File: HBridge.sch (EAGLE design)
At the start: 42 parts, among them IC1 74HC08D, IC2 A4954, J1 In 3/4, J2 Power, J3 In 1/2, J4 Output A, J5 Output B, J6 Digital_8_13, J7 Analog, J8 Digital_0_7

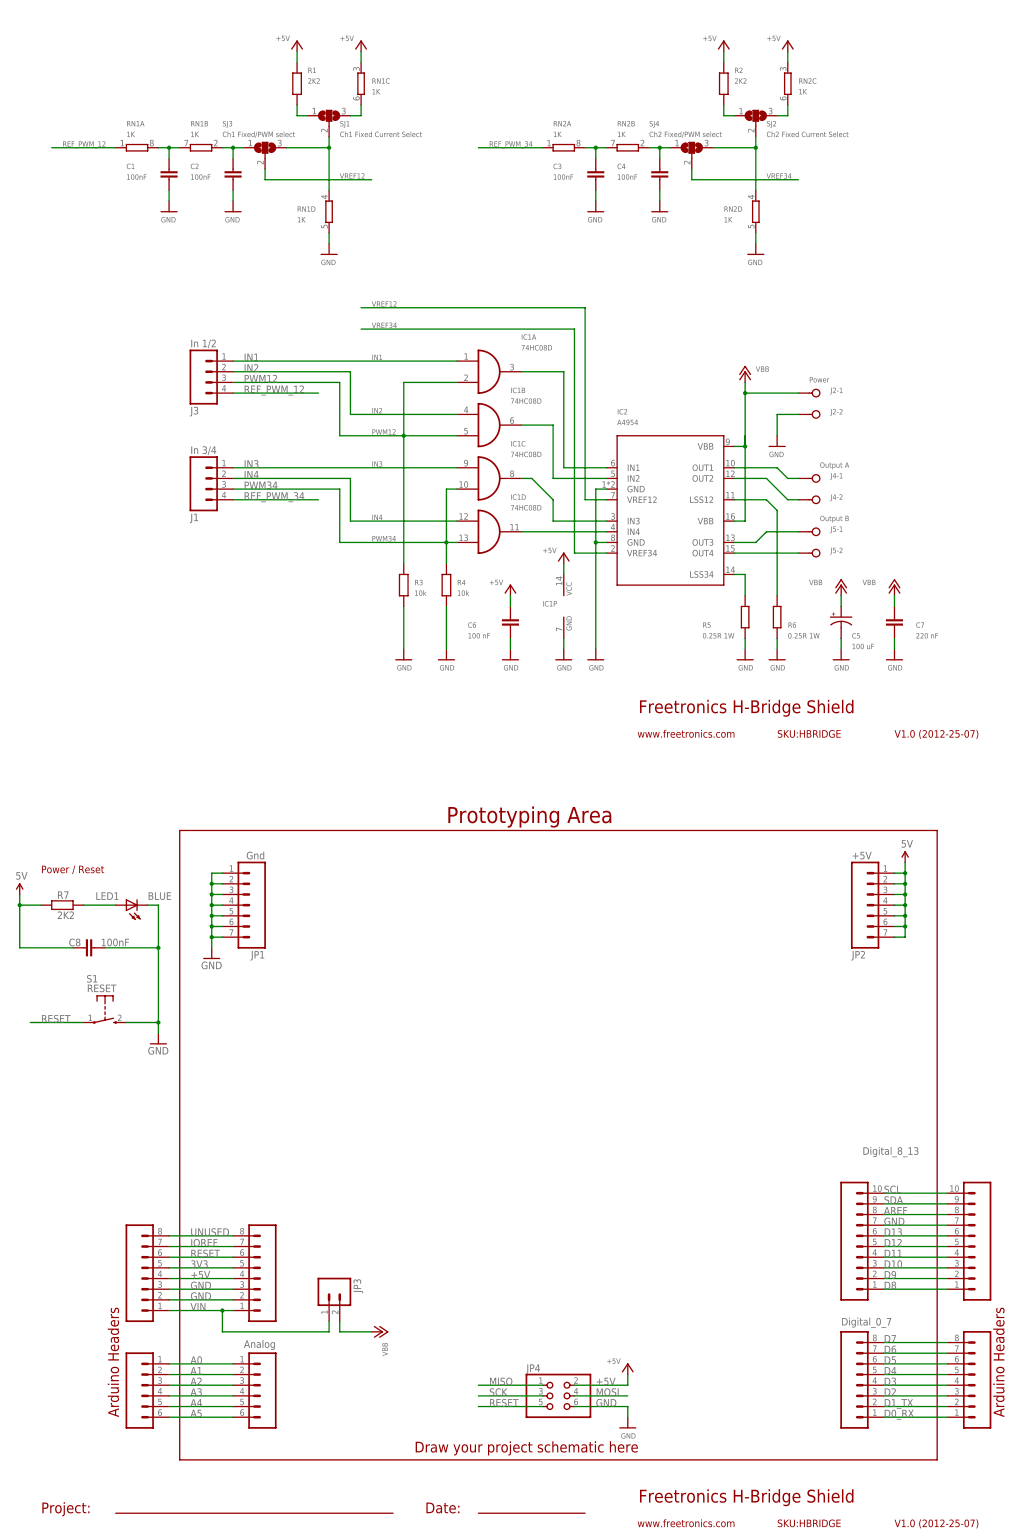
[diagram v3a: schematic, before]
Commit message: Made track widths consistent; renamed parts; relocated designators, improved silkscreen
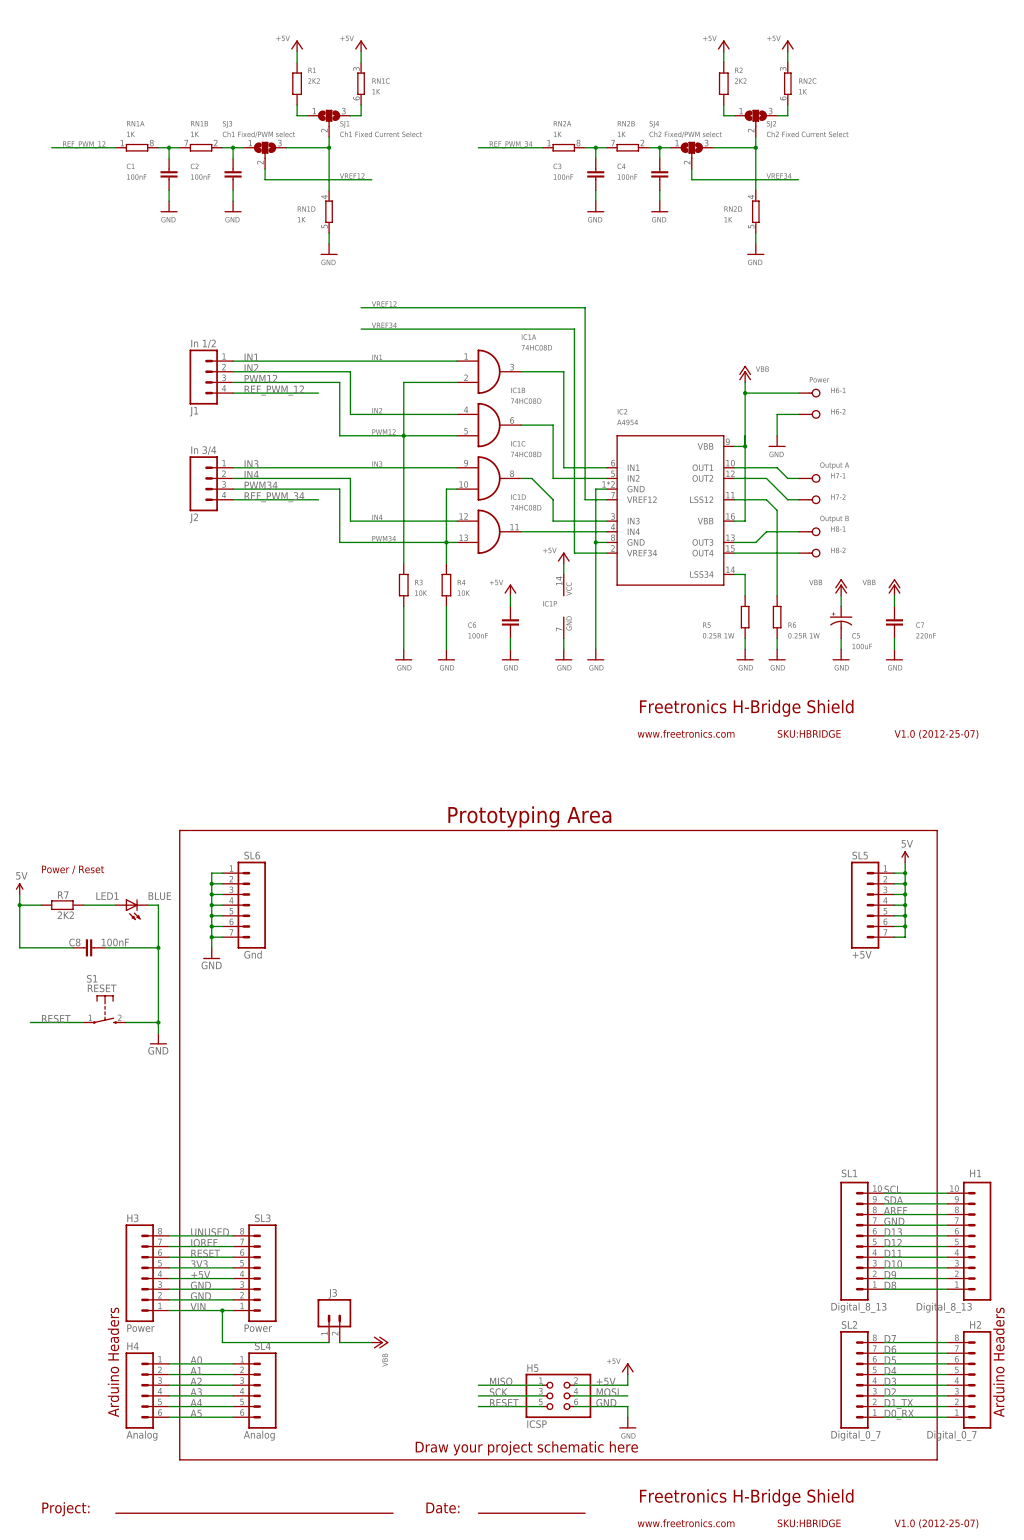
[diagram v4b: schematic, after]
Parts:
- removed JP2: +5V, SparkFun:M07
- removed JP3: (no value), freetronics-master-v1:M02PTH
- added H3: Power, freetronics:M08
- added H6: Power, con-wago-508:W237-02P
- C5: value 100 uF -> 100uF
- C6: value 100 nF -> 100nF
- C7: value 220 nF -> 220nF
- H5: value (none) -> ICSP
- J1: value In 3/4 -> In 1/2
- J2: value Power -> In 3/4; device con-wago-508:W237-02P -> freetronics-master-v1:M04PTH
- J3: value In 1/2 -> (none); device freetronics-master-v1:M04PTH -> freetronics-master-v1:M02PTH
- R3, R4: value 10k -> 10K
- SL2: value Analog -> Digital_0_7; device freetronics:M06SIP -> freetronics:M08
- SL3: value Digital_0_7 -> Power
- SL4: value Digital_0_7 -> Analog; device freetronics:M08 -> freetronics:M06SIP
- SL5: value Digital_0_7 -> +5V; device freetronics:M08 -> SparkFun:M07
- renumbered J4 to H7, J5 to H8, J6 to H1, J7 to H4, J8 to H2, JP1 to SL6, JP4 to H5
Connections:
- net +5V: now also H3.4, SL3.4, SL5.1, SL5.2, SL5.3, SL5.5, SL5.6, SL5.7; no longer JP2.1, JP2.2, JP2.3, JP2.4, JP2.5, JP2.6, JP2.7, SL4.4
- net 3V3: now also H3.5, SL3.5; no longer SL4.5, SL5.5
- net A0: now also SL4.1; no longer SL2.1
- net A1: now also SL4.2; no longer SL2.2
- net A2: now also SL4.3; no longer SL2.3
- net A3: now also SL4.4; no longer SL2.4
- net A4: now also SL4.5; no longer SL2.5
- net A5: now also SL4.6; no longer SL2.6
- net D0_RX: now also SL2.1; no longer SL3.1
- net D1_TX: now also SL2.2; no longer SL3.2
- net D2: now also SL2.3; no longer SL3.3
- net D3: now also SL2.4; no longer SL3.4
- net D4: now also SL2.5; no longer SL3.5
- net D5: now also SL2.6; no longer SL3.6
- net D6: now also SL2.7; no longer SL3.7
- net D7: now also SL2.8; no longer SL3.8
- net GND: now also H3.2, H3.3, H6-2.KL, SL3.2, SL3.3; no longer J2-2.KL, SL4.2, SL4.3, SL5.2, SL5.3
- net IN1: now also J1.1; no longer J3.1
- net IN2: now also J1.2; no longer J3.2
- net IN3: now also J2.1; no longer J1.1
- net IN4: now also J2.2; no longer J1.2
- net IOREF: now also H3.7, SL3.7; no longer SL4.7, SL5.7
- net PWM12: now also J1.3; no longer J3.3
- net PWM34: now also J2.3; no longer J1.3
- net REF_PWM_12: now also J1.4; no longer J3.4
- net REF_PWM_34: now also J2.4; no longer J1.4
- net RESET: now also H3.6, SL3.6; no longer SL4.6, SL5.6
- net UNUSED: now also H3.8, SL3.8; no longer SL4.8, SL5.8
- net VBB: now also H6-1.KL, J3.2; no longer J2-1.KL, JP3.2
- net VIN: now also H3.1, J3.1, SL3.1; no longer JP3.1, SL4.1, SL5.1
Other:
- moved on the sheet: J1

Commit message: Restructured schematic and board for switchable current limit
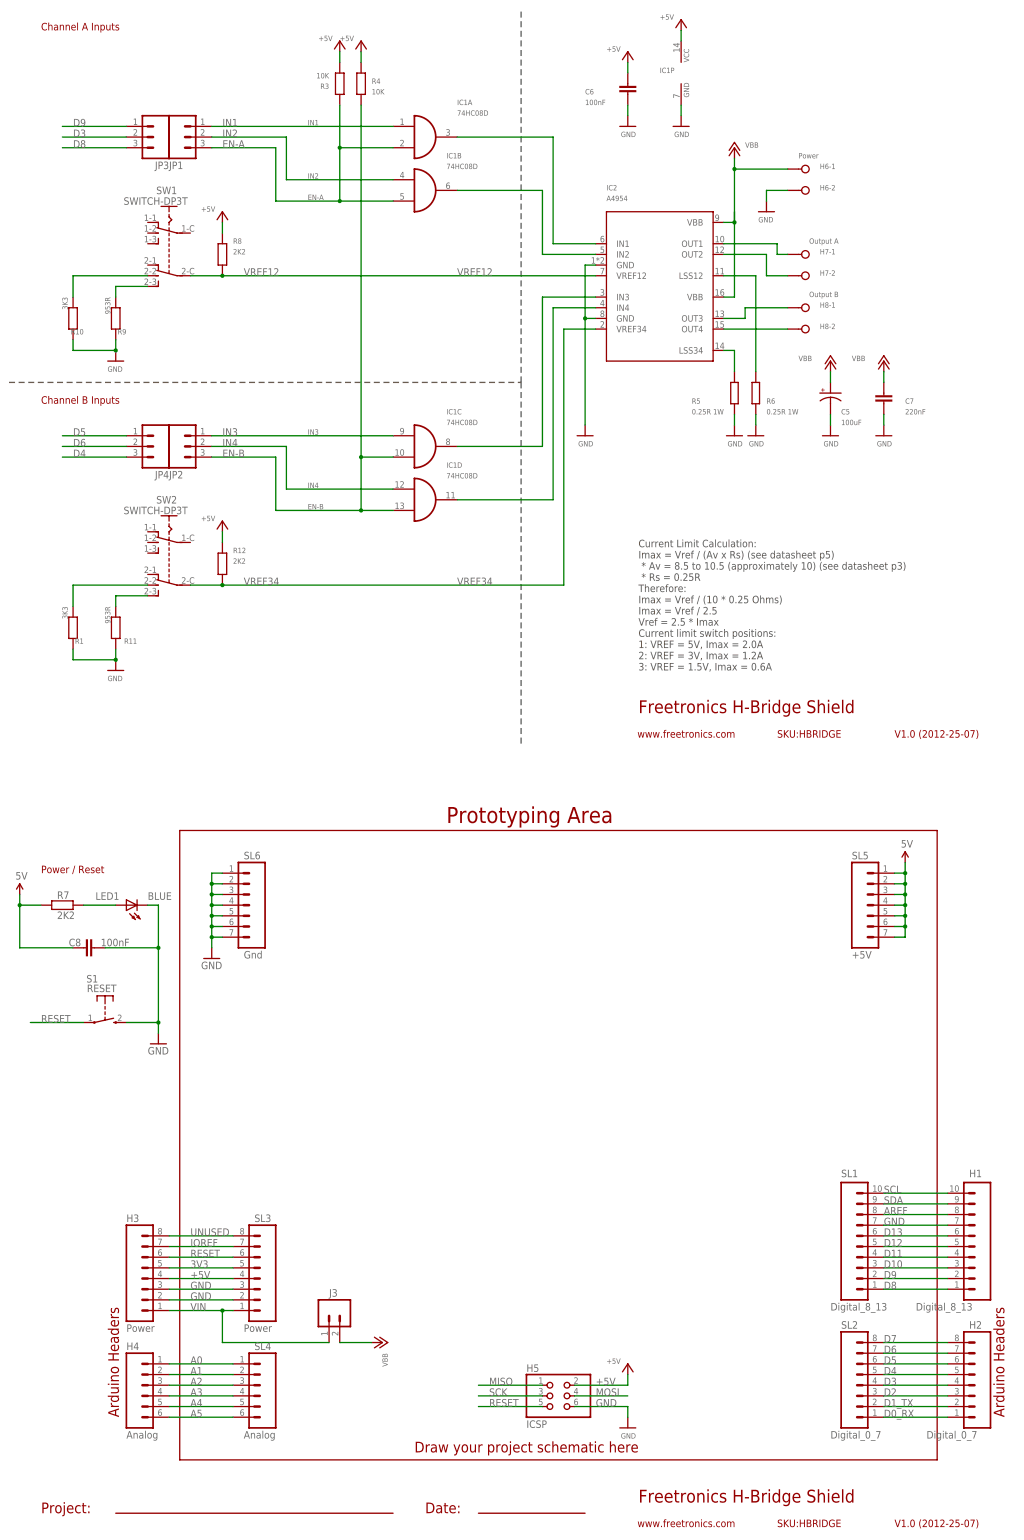
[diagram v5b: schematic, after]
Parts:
- removed C1, C2, C3, C4: 100nF, freetronics-master-v1:CAP0603
- removed J1: In 1/2, freetronics-master-v1:M04PTH
- removed J2: In 3/4, freetronics-master-v1:M04PTH
- removed R2: 2K2, freetronics-master-v1:RESISTOR0603
- removed RN1, RN2: 1K, freetronics-master-v1:4R-NCAY16
- removed SJ1: Ch1 Fixed Current Select, freetronics-master-v1:SJ2W
- removed SJ2: Ch2 Fixed Current Select, freetronics-master-v1:SJ2W
- removed SJ3: Ch1 Fixed/PWM select, freetronics-master-v1:SJ2W
- removed SJ4: Ch2 Fixed/PWM select, freetronics-master-v1:SJ2W
- added JP1, JP2, JP3, JP4: (no value), freetronics-master-v1.1:M03PTH
- added R10: 3K3, freetronics-master-v1:RESISTOR0603
- added R11, R9: 953R, freetronics-master-v1:RESISTOR0603
- added R12, R8: 2K2, freetronics-master-v1:RESISTOR0603
- added SW1, SW2: SWITCH-DP3T, freetronics-jon:SWITCH-DP3T
- R1: value 2K2 -> 3K3
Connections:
- removed net N$1: RN2D.1, SJ2.2, SJ4.3
- removed net N$16: RN1D.1, SJ1.2, SJ3.3
- removed net N$17: R2.1, SJ2.1
- removed net N$18: C2.1, RN1B.1, SJ3.1
- removed net N$19: C1.1, RN1A.2, RN1B.2
- removed net N$2: C4.1, RN2B.1, SJ4.1
- removed net N$20: RN2C.2, SJ2.3
- removed net N$3: C3.1, RN2A.2, RN2B.2
- removed net PWM12: IC1A.I1, IC1B.I1, J1.3, R3.2
- removed net PWM34: IC1C.I1, IC1D.I1, J2.3, R4.2
- removed net REF_PWM_12: J1.4, RN1A.1
- removed net REF_PWM_34: J2.4, RN2A.1
- new net EN-A: IC1A.I1, IC1B.I1, JP1.3, R3.2
- new net EN-B: IC1C.I1, IC1D.I1, JP2.3, R4.1
- new net N$21: R9.1, SW1.2-3
- new net N$49: R1.1, SW2.2-2
- net +5V: now also R12.1, R3.1, R4.2, R8.1; no longer R1.2, R2.2, RN1C.1, RN2C.1
- net D3: now also JP3.2
- net D4: now also JP4.3
- net D5: now also JP4.1
- net D6: now also JP4.2
- net D8: now also JP3.3
- net D9: now also JP3.1
- net GND: now also R1.2, R10.2, R11.2, R9.2; no longer C1.2, C2.2, C3.2, C4.2, R3.1, R4.1, RN1D.2, RN2D.2
- net IN1: now also JP1.1; no longer J1.1
- net IN2: now also JP1.2; no longer J1.2
- net IN3: now also JP2.1; no longer J2.1
- net IN4: now also JP2.2; no longer J2.2
- net N$15: now also R10.1, SW1.2-2; no longer RN1C.2, SJ1.3
- net N$4: now also R11.1, SW2.2-3; no longer R1.1, SJ1.1
- net VREF12: now also R8.2, SW1.2-C; no longer SJ3.2
- net VREF34: now also R12.2, SW2.2-C; no longer SJ4.2
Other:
- note added: "2A max."
- note added: "Channel A Inputs"
- note added: "Channel B Inputs"
- note added: "Current Limit Calculation: Imax = Vref / (Av x Rs) (see datasheet p5) * Av = 8.5 to 10.5 (approximately 10) (see datasheet p3) * Rs = 0.25R Therefore: Imax = Vref / (10 * 0.25 Ohms) Imax = Vref / 2.5 Vref = 2.5 * Imax Current limit switch positions: 1: VREF = 5V, Imax = 2.0A 2: VREF = 3V, Imax = 1.2A 3: VREF = 1.5V, Imax = 0.6A"
- note removed: "1-2-3: 2.96V, I = 1.19A"
- note removed: "1-2: 1.56V, I = 625mA"
- note removed: "1k resistor networks: Small SMD 4-way resistor pack, SAME package footprint as EM."
- note removed: "2 A max."
- note removed: "2-3: 2.5V, I = 1A"
- note removed: "I limit = Vref / (0.25 ohms * 10)"
- moved on the sheet: C5, C6, C7, H6-1, H6-2, H7-1, H7-2, H8-1, H8-2, IC1A, IC1B, IC1C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
